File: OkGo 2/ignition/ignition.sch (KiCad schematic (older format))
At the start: 42 parts, among them K101 16A SPST, P101 BATT, P102 BATT, P103 CHARGE_CASE, P104 CHARGE_CASE, P105 CHARGE_JST_XH, P106 SMA, SW101 LATCHING PUSH, U101 FUSE 15A, U102 SWD, U103 CLIP, U104 BEZEL, U105 RFM95W, U106 STM32F071CBT6, U107 TSR 0.5-2433, Y101 8MHz

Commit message: Flyback diodes, fixes #18
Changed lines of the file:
@@
 Connection ~ 6425 1000
 Wire Wire Line
-	7150 1250 7150 1300
-Wire Wire Line
-	7150 1300 7150 1350
+	7150 1250 7150 1350
 Wire Wire Line
 	7150 1700 7150 1650
@@
 	9250 1550 9350 1550
 Wire Wire Line
-	9250 1250 9250 1350
-Wire Wire Line
-	9250 1350 9250 1550
-Wire Wire Line
-	9250 1550 9250 1600
+	9250 1250 9250 1600
 Wire Wire Line
 	9350 1350 9250 1350
@@
 	10600 1550 10550 1550
 Wire Wire Line
-	8300 5350 8375 5350
-Wire Wire Line
-	8375 5350 8600 5350
-Wire Wire Line
-	8600 5350 8700 5350
-Wire Wire Line
-	8700 5350 8750 5350
-Wire Wire Line
-	8750 5350 8800 5350
+	8300 5350 8800 5350
 Wire Wire Line
 	8700 5350 8700 5450
@@
 Connection ~ 8750 5350
 Wire Wire Line
-	8600 4875 8600 4925
-Wire Wire Line
-	8600 4925 8600 4975
-Wire Wire Line
-	8375 4925 8600 4925
-Wire Wire Line
-	8600 4925 8800 4925
+	8600 4875 8600 4975
+Wire Wire Line
+	8375 4925 8800 4925
 Wire Wire Line
 	8800 4925 8800 5150
@@
 Connection ~ 8600 5350
 Wire Wire Line
-	10275 6150 10350 6150
-Wire Wire Line
-	10350 6150 10425 6150
-Wire Wire Line
-	10275 6150 10275 6275
-Wire Wire Line
-	10275 6275 10275 6300
-Wire Wire Line
-	10000 6050 10075 6050
-Wire Wire Line
-	10075 6050 10425 6050
+	10275 6150 10425 6150
+Wire Wire Line
+	10275 6150 10275 6300
+Wire Wire Line
+	10000 6050 10425 6050
 Wire Wire Line
 	1450 5100 1400 5100
 Wire Wire Line
-	1450 3950 1450 4100
-Wire Wire Line
-	1450 4100 1450 4200
-Wire Wire Line
-	1450 4200 1450 4300
-Wire Wire Line
-	1450 4300 1450 4400
-Wire Wire Line
-	1450 4400 1450 4500
-Wire Wire Line
-	1450 4500 1450 4700
-Wire Wire Line
-	1450 4700 1450 4800
-Wire Wire Line
-	1450 4800 1450 4900
-Wire Wire Line
-	1450 4900 1450 5100
-Wire Wire Line
-	1450 5100 1450 5200
-Wire Wire Line
-	1450 5200 1450 5300
+	1450 3950 1450 5300
 Connection ~ 1450 4300
 Connection ~ 1450 4500
@@
 	1000 5100 1100 5100
 Wire Wire Line
-	1000 4100 1000 4300
-Wire Wire Line
-	1000 4300 1000 4500
-Wire Wire Line
-	1000 4500 1000 4700
-Wire Wire Line
-	1000 4700 1000 4900
-Wire Wire Line
-	1000 4900 1000 5100
-Wire Wire Line
-	1000 5100 1000 5300
-Wire Wire Line
-	1000 5300 1000 5450
+	1000 4100 1000 5450
 Wire Wire Line
 	1000 4900 1100 4900
@@
 Connection ~ 1000 4500
 Wire Wire Line
-	1000 5450 1500 5450
-Wire Wire Line
-	1500 5450 1800 5450
-Wire Wire Line
-	1800 5450 1850 5450
-Wire Wire Line
-	1850 5450 1900 5450
-Wire Wire Line
-	1900 5450 1950 5450
+	1000 5450 1950 5450
 Wire Wire Line
 	1900 5450 1900 5350
@@
 Connection ~ 1800 5450
 Wire Wire Line
-	3850 4750 3950 4750
-Wire Wire Line
-	3950 4750 4000 4750
+	3850 4750 4000 4750
 Wire Wire Line
 	3950 4750 3950 4800
 Connection ~ 3950 4750
 Wire Wire Line
-	3750 4450 3850 4450
-Wire Wire Line
-	3850 4450 4000 4450
-Wire Wire Line
-	4000 4450 4200 4450
+	3750 4450 4200 4450
 Wire Wire Line
 	3750 4450 3750 4700
@@
 	4100 5300 4100 5200
 Wire Wire Line
-	4100 5200 4350 5200
-Wire Wire Line
-	4350 5200 4850 5200
-Wire Wire Line
-	4100 5500 4350 5500
-Wire Wire Line
-	4350 5500 4650 5500
+	4100 5200 4850 5200
+Wire Wire Line
+	4100 5500 4650 5500
 Wire Wire Line
 	4100 5500 4100 5400
@@
 	4850 5950 4850 5850
 Wire Wire Line
-	4650 5950 4750 5950
-Wire Wire Line
-	4750 5950 4850 5950
+	4650 5950 4850 5950
 Wire Wire Line
 	4650 5950 4650 5850
@@
 	1500 5450 1500 5500
 Wire Wire Line
-	6450 6400 6550 6400
-Wire Wire Line
-	6550 6400 6650 6400
+	6450 6400 6650 6400
 Wire Wire Line
 	1900 4500 1900 4550
@@
 	4550 1100 4550 1150
 Wire Wire Line
-	4550 950  4600 950
-Wire Wire Line
-	4600 950  4650 950
+	4550 950  4650 950
 Wire Wire Line
 	4600 950  4600 950
 Connection ~ 4600 950
 Wire Wire Line
-	4550 1150 4600 1150
-Wire Wire Line
-	4600 1150 6200 1150
+	4550 1150 6200 1150
 Wire Wire Line
 	4600 1150 4600 1150
@@
 Connection ~ 10350 6150
 Wire Wire Line
-	10375 5850 10375 5900
-Wire Wire Line
-	10375 5900 10375 5950
+	10375 5850 10375 5950
 Wire Wire Line
 	10375 5900 10425 5900
@@
 	3300 750  3300 1000
 Wire Wire Line
-	3300 1000 3450 1000
-Wire Wire Line
-	3450 1000 3950 1000
+	3300 1000 3950 1000
 Connection ~ 3150 750
 Wire Wire Line
@@
 Connection ~ 2850 1250
 Wire Wire Line
-	2600 750  3150 750
-Wire Wire Line
-	3150 750  3300 750
-Wire Wire Line
-	2600 1250 2850 1250
-Wire Wire Line
-	2850 1250 3300 1250
+	2600 750  3300 750
+Wire Wire Line
+	2600 1250 3300 1250
 Wire Wire Line
 	6950 1000 6950 1050
@@
 	3150 1950 3150 1900
 Wire Wire Line
-	6050 900  6425 900
-Wire Wire Line
-	6425 900  6700 900
-Wire Wire Line
-	6700 900  6950 900
-Wire Wire Line
-	6950 900  7150 900
+	6050 900  7150 900
 Wire Wire Line
 	5450 6300 5450 6400
@@
 	3300 1100 3950 1100
 Wire Wire Line
-	6200 1000 6425 1000
-Wire Wire Line
-	6425 1000 6700 1000
-Wire Wire Line
-	6700 1000 6950 1000
+	6200 1000 6950 1000
 Wire Wire Line
 	4650 1000 4700 1000

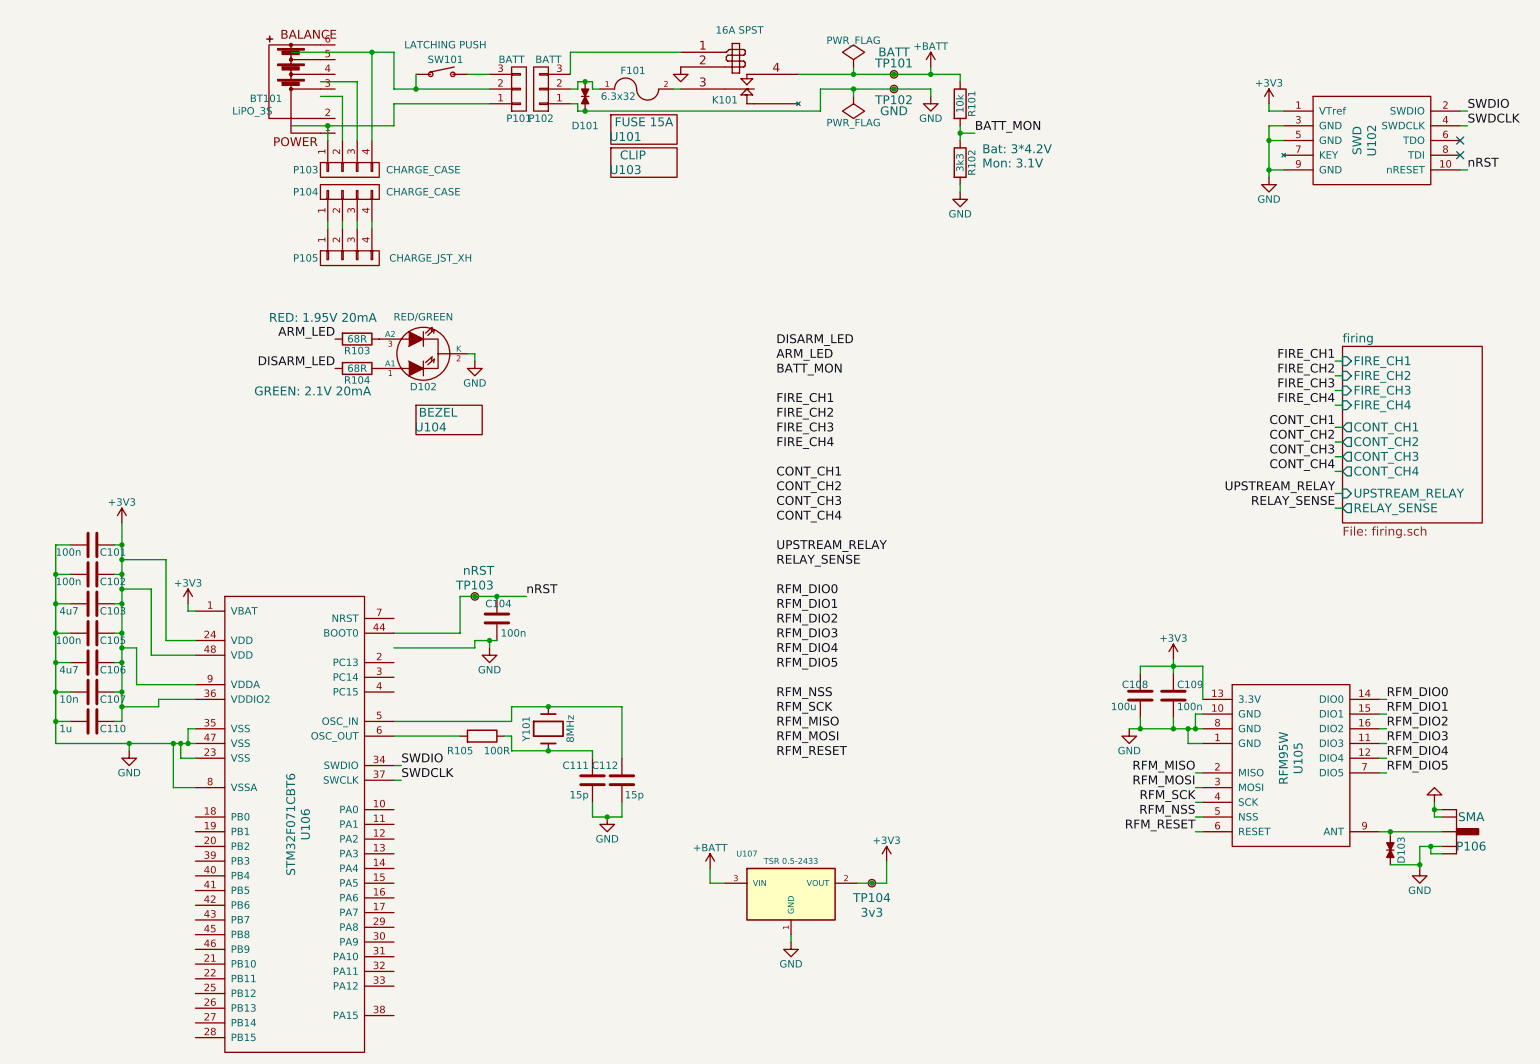
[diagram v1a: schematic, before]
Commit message: Lots more footprinting, mostly done.
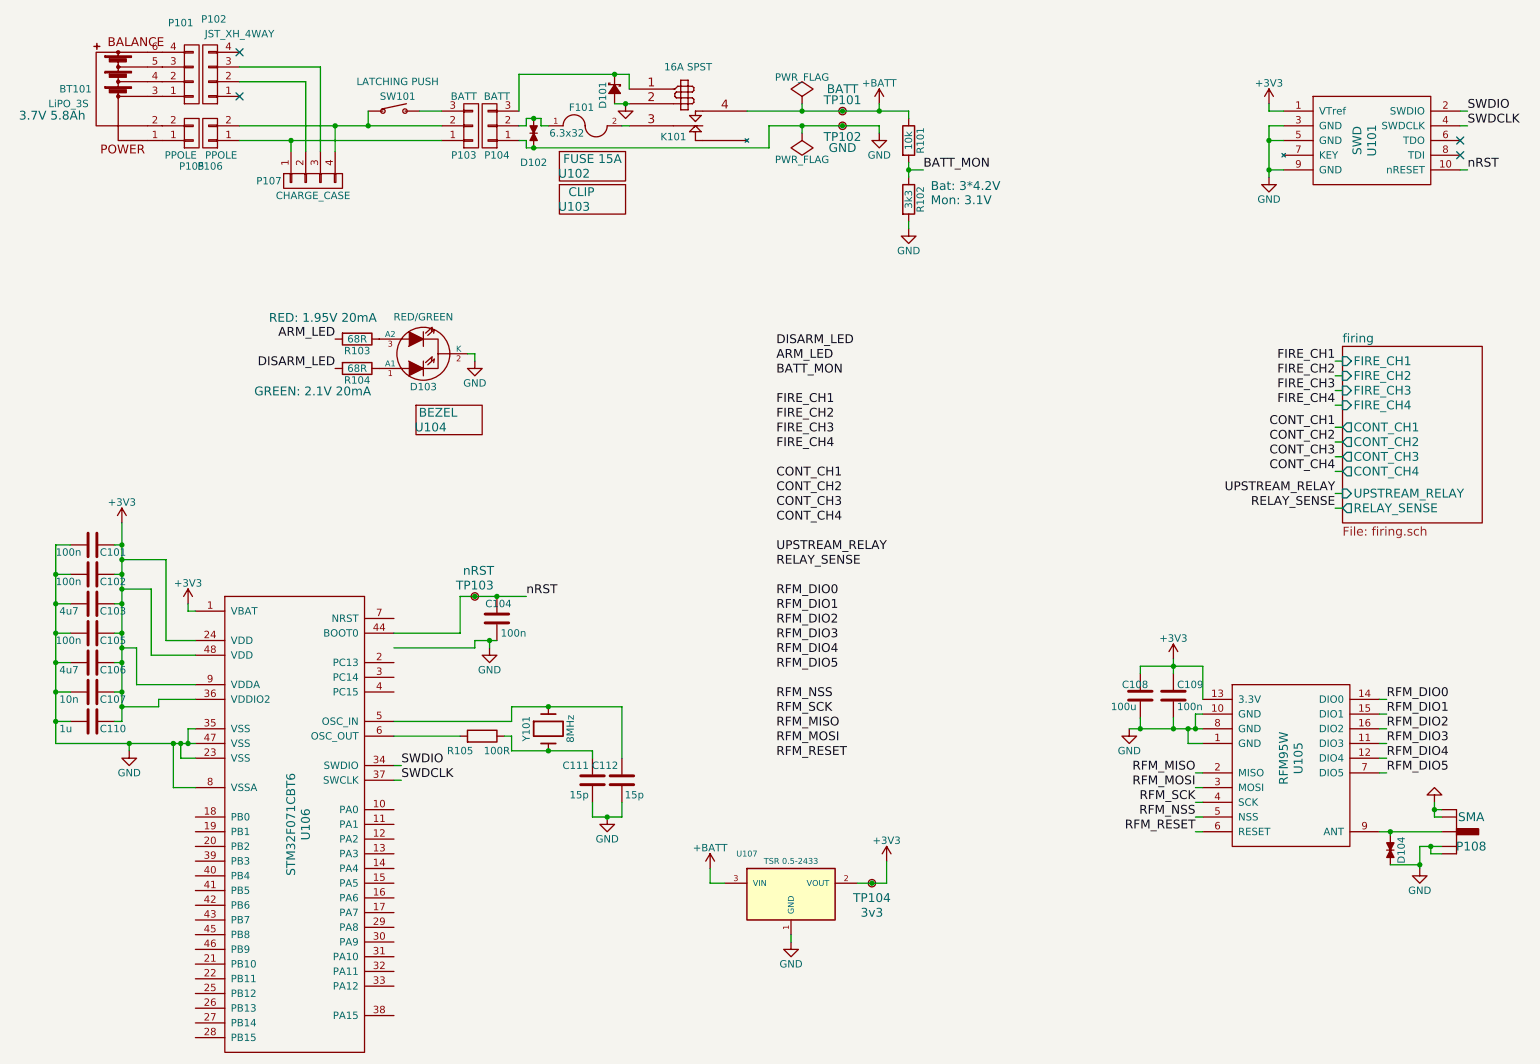
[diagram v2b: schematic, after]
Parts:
- removed P104: CHARGE_CASE, symbol CONN_01X04
- removed P105: CHARGE_JST_XH, symbol CONN_01X04
- added D101: MBR2H200SFT1G, ignition:SOD-123FL, symbol D_Schottky_Small
- added P101: ~, symbol CONN_01X04
- added P102: JST_XH_4WAY, symbol CONN_01X04
- added P105, P106: PPOLE, symbol CONN_01X02
- BT101: URL http://hobbyking.com/hobbyking/store/uh_viewItem.asp?idProduct=21380 -> http://hobbyking.com/hobbyking/store/uh_viewItem.asp?idProduct=34640
- K101: footprint (none) -> ignition:Relay_RT314
- renumbered D101 to D102, D102 to D103, D103 to D104, P101 to P103, P102 to P104, P103 to P107, P106 to P108, U102 to U101, U101 to U102
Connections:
- net GND: now also D101.2 (A)
- net at BT101.1: now also P105.1 (P1)
- net at BT101.2: now also P105.2 (P2)
- net at BT101.3: now also P101.1 (P1)
- net at BT101.4: now also P101.2 (P2)
- net at BT101.5: now also P101.3 (P3)
- net at BT101.6: now also P101.4 (P4)
- net at P103.1 (P1), P107.1 (P1): now also P106.1 (P1)
- net at P107.2 (P2): now also P102.2 (P2)
- net at P107.3 (P3): now also P102.3 (P3)
- net at P103.2 (P2), P107.4 (P4), SW101.1: now also P106.2 (P2)
- net at K101.1, P104.3 (P3): now also D101.1 (K)
- no-connect marks 2 -> 4
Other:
- note added: "3.7V 5.8Ah"
- moved on the sheet: BT101, D102, F101, K101, P103, P104, P107, R101, R102, SW101, TP101, TP102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

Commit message: Non-handsoldering footprints, fixes #17
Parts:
- C101, C102, C103, C104, C105, C106, C107, C109, C110, C111, C112: footprint Capacitors_SMD:C_0805_HandSoldering -> Capacitors_SMD:C_0805
- C108: footprint Capacitors_SMD:C_1206_HandSoldering -> Capacitors_SMD:C_1206
- D102, D104: footprint Resistors_SMD:R_0603_HandSoldering -> Resistors_SMD:R_0603
- R101, R102, R103, R104, R105: footprint Resistors_SMD:R_0805_HandSoldering -> Resistors_SMD:R_0805
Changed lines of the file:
@@
 F 0 "R101" V 6880 1350 50  0000 C CNN
 F 1 "10k" V 6800 1350 50  0000 C CNN
-F 2 "Resistors_SMD:R_0805_HandSoldering" V 6730 1350 30  0001 C CNN
+F 2 "Resistors_SMD:R_0805" V 6730 1350 30  0001 C CNN
 F 3 "" H 6800 1350 30  0000 C CNN
 F 4 "9237755" H 6800 1350 60  0001 C CNN "Farnell"
@@
 F 0 "R102" V 6880 1750 50  0000 C CNN
 F 1 "3k3" V 6800 1750 50  0000 C CNN
-F 2 "Resistors_SMD:R_0805_HandSoldering" V 6730 1750 30  0001 C CNN
+F 2 "Resistors_SMD:R_0805" V 6730 1750 30  0001 C CNN
 F 3 "" H 6800 1750 30  0000 C CNN
 F 4 "9237682" H 6800 1750 60  0001 C CNN "Farnell"
@@
 F 0 "C109" H 8625 5200 50  0000 L CNN
 F 1 "100n" H 8625 5050 50  0000 L CNN
-F 2 "Capacitors_SMD:C_0805_HandSoldering" H 8638 4975 30  0001 C CNN
+F 2 "Capacitors_SMD:C_0805" H 8638 4975 30  0001 C CNN
 F 3 "" H 8600 5125 60  0000 C CNN
 F 4 "2407344" H 8600 5125 60  0001 C CNN "Farnell"
@@
 F 0 "C105" V 1300 4750 50  0000 L CNN
 F 1 "100n" V 1300 4450 50  0000 L CNN
-F 2 "Capacitors_SMD:C_0805_HandSoldering" H 1288 4550 30  0001 C CNN
+F 2 "Capacitors_SMD:C_0805" H 1288 4550 30  0001 C CNN
 F 3 "" H 1250 4700 60  0000 C CNN
 F 4 "2407344" H 1250 4700 60  0001 C CNN "Farnell"
@@
 F 0 "C107" V 1300 5150 50  0000 L CNN
 F 1 "10n" V 1300 4875 50  0000 L CNN
-F 2 "Capacitors_SMD:C_0805_HandSoldering" H 1288 4950 30  0001 C CNN
+F 2 "Capacitors_SMD:C_0805" H 1288 4950 30  0001 C CNN
 F 3 "" H 1250 5100 60  0000 C CNN
 F 4 "2407341" H 1250 5100 60  0001 C CNN "Farnell"
@@
 F 0 "C104" H 3900 4700 50  0000 L CNN
 F 1 "100n" H 3800 4500 50  0000 L CNN
-F 2 "Capacitors_SMD:C_0805_HandSoldering" H 4038 4450 30  0001 C CNN
+F 2 "Capacitors_SMD:C_0805" H 4038 4450 30  0001 C CNN
 F 3 "" H 4000 4600 60  0000 C CNN
 F 4 "2407344" H 4000 4600 60  0001 C CNN "Farnell"
@@
 F 0 "R105" V 3800 5250 50  0000 C CNN
 F 1 "100R" V 3800 5500 50  0000 C CNN
-F 2 "Resistors_SMD:R_0805_HandSoldering" V 3830 5400 30  0001 C CNN
+F 2 "Resistors_SMD:R_0805" V 3830 5400 30  0001 C CNN
 F 3 "" H 3900 5400 30  0000 C CNN
 F 4 "2331783" H 3900 5400 60  0001 C CNN "Farnell"
@@
 F 0 "C111" H 4675 5800 50  0000 L CNN
 F 1 "15p" H 4675 5600 50  0000 L CNN
-F 2 "Capacitors_SMD:C_0805_HandSoldering" H 4688 5550 30  0001 C CNN
+F 2 "Capacitors_SMD:C_0805" H 4688 5550 30  0001 C CNN
 F 3 "" H 4650 5700 60  0000 C CNN
 F 4 "1414668" H 4650 5700 60  0001 C CNN "Farnell"
@@
 F 0 "C112" H 4875 5800 50  0000 L CNN
 F 1 "15p" H 4700 5600 50  0000 L CNN
-F 2 "Capacitors_SMD:C_0805_HandSoldering" H 4888 5550 30  0001 C CNN
+F 2 "Capacitors_SMD:C_0805" H 4888 5550 30  0001 C CNN
 F 3 "" H 4850 5700 60  0000 C CNN
 F 4 "1414668" H 4850 5700 60  0001 C CNN "Farnell"
@@
 F 0 "C102" V 1300 4350 50  0000 L CNN
 F 1 "100n" V 1300 4050 50  0000 L CNN
-F 2 "Capacitors_SMD:C_0805_HandSoldering" H 1288 4150 30  0001 C CNN
+F 2 "Capacitors_SMD:C_0805" H 1288 4150 30  0001 C CNN
 F 3 "" H 1250 4300 60  0000 C CNN
 F 4 "2407344" H 1250 4300 60  0001 C CNN "Farnell"
@@
 F 0 "C101" V 1300 4150 50  0000 L CNN
 F 1 "100n" V 1300 3850 50  0000 L CNN
-F 2 "Capacitors_SMD:C_0805_HandSoldering" H 1288 3950 30  0001 C CNN
+F 2 "Capacitors_SMD:C_0805" H 1288 3950 30  0001 C CNN
 F 3 "" H 1250 4100 60  0000 C CNN
 F 4 "2407344" H 1250 4100 60  0001 C CNN "Farnell"
@@
 F 0 "C110" V 1300 5350 50  0000 L CNN
 F 1 "1u" V 1300 5075 50  0000 L CNN
-F 2 "Capacitors_SMD:C_0805_HandSoldering" H 1288 5150 30  0001 C CNN
+F 2 "Capacitors_SMD:C_0805" H 1288 5150 30  0001 C CNN
 F 3 "" H 1250 5300 60  0000 C CNN
 F 4 "9227792" H 1250 5300 60  0001 C CNN "Farnell"
@@
 F 0 "C106" V 1300 4950 50  0000 L CNN
 F 1 "4u7" V 1300 4675 50  0000 L CNN
-F 2 "Capacitors_SMD:C_0805_HandSoldering" H 1288 4750 30  0001 C CNN
+F 2 "Capacitors_SMD:C_0805" H 1288 4750 30  0001 C CNN
 F 3 "" H 1250 4900 60  0000 C CNN
 F 4 "1845742" H 1250 4900 60  0001 C CNN "Farnell"
@@
 F 0 "C103" V 1300 4550 50  0000 L CNN
 F 1 "4u7" V 1300 4275 50  0000 L CNN
-F 2 "Capacitors_SMD:C_0805_HandSoldering" H 1288 4350 30  0001 C CNN
+F 2 "Capacitors_SMD:C_0805" H 1288 4350 30  0001 C CNN
 F 3 "" H 1250 4500 60  0000 C CNN
 F 4 "1845742" H 1250 4500 60  0001 C CNN "Farnell"
@@
 F 0 "C108" H 8250 5200 50  0000 L CNN
 F 1 "100u" H 8175 5050 50  0000 L CNN
-F 2 "Capacitors_SMD:C_1206_HandSoldering" H 8413 4975 30  0001 C CNN
+F 2 "Capacitors_SMD:C_1206" H 8413 4975 30  0001 C CNN
 F 3 "" H 8375 5125 60  0000 C CNN
 F 4 "2362115" H 8375 5125 60  0001 C CNN "Farnell"
@@
 F 0 "D102" V 4450 1300 50  0000 C CNN
 F 1 "TVS_small" H 4250 1225 50  0001 C CNN
-F 2 "Resistors_SMD:R_0603_HandSoldering" H 4250 1300 60  0001 C CNN
+F 2 "Resistors_SMD:R_0603" H 4250 1300 60  0001 C CNN
 F 3 "" H 4250 1300 60  0000 C CNN
 F 4 "2368174" H 4250 1300 60  0001 C CNN "Farnell"
@@
 F 0 "D104" H 10075 6250 50  0000 C CNN
 F 1 "TVS_small" H 10075 6100 50  0001 C CNN
-F 2 "Resistors_SMD:R_0603_HandSoldering" H 10075 6175 60  0001 C CNN
+F 2 "Resistors_SMD:R_0603" H 10075 6175 60  0001 C CNN
 F 3 "" H 10075 6175 60  0000 C CNN
 F 4 "2368174" H 10075 6175 60  0001 C CNN "Farnell"
@@
 F 0 "R103" V 3130 2700 50  0000 C CNN
 F 1 "68R" V 3050 2700 50  0000 C CNN
-F 2 "Resistors_SMD:R_0805_HandSoldering" V 2980 2700 30  0001 C CNN
+F 2 "Resistors_SMD:R_0805" V 2980 2700 30  0001 C CNN
 F 3 "" H 3050 2700 30  0000 C CNN
 F 4 "2332055" H 3050 2700 60  0001 C CNN "Farnell"
@@
 F 0 "R104" V 3130 2900 50  0000 C CNN
 F 1 "68R" V 3050 2900 50  0000 C CNN
-F 2 "Resistors_SMD:R_0805_HandSoldering" V 2980 2900 30  0001 C CNN
+F 2 "Resistors_SMD:R_0805" V 2980 2900 30  0001 C CNN
 F 3 "" H 3050 2900 30  0000 C CNN
 F 4 "2332055" H 3050 2900 60  0001 C CNN "Farnell"
